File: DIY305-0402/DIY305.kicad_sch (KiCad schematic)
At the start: 37 parts, among them J4 Conn_02x07_Counter_Clockwise

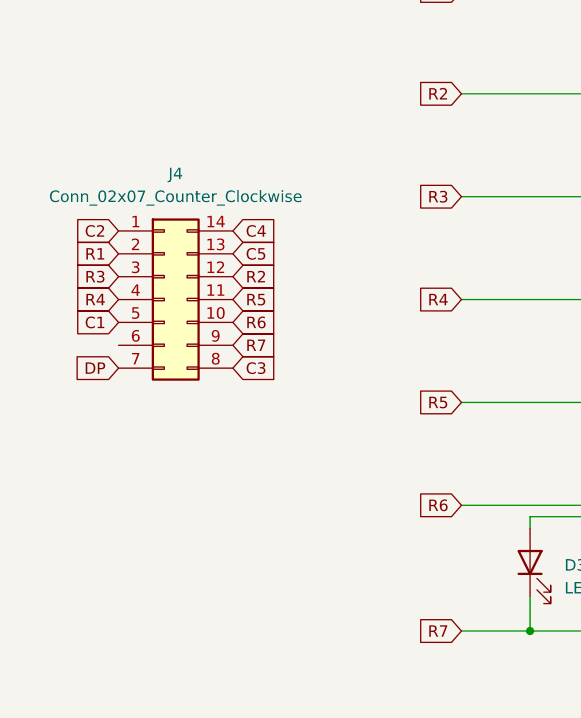
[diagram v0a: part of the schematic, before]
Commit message: Removal of old design
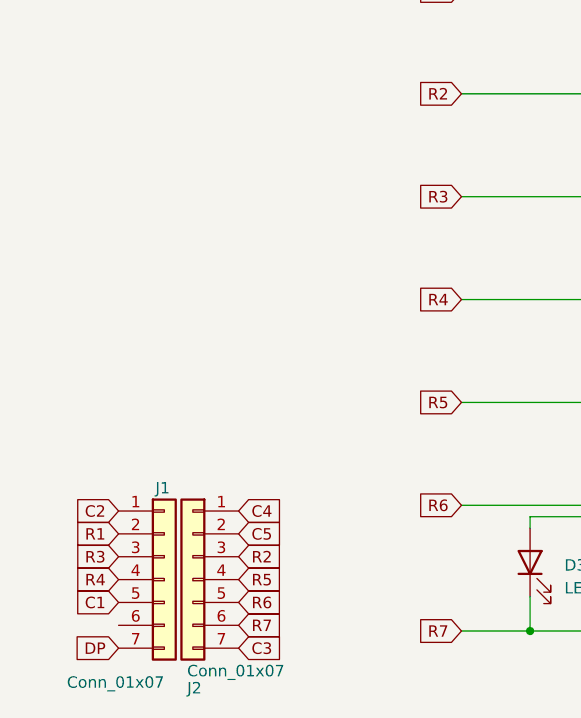
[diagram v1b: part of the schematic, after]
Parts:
- removed J4: Conn_02x07_Counter_Clockwise, symbol Connector_Generic:Conn_02x07_Counter_Clockwise
- added J1, J2: Conn_01x07, Connector_PinHeader_2.54mm:PinHeader_1x07_P2.54mm_Vertical, symbol Connector_Generic:Conn_01x07
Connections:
- net C1: now also J2.5 (Pin_5)
- net C2: now also J2.1 (Pin_1)
- net C3: now also J1.7 (Pin_7)
- net C4: now also J1.1 (Pin_1)
- net C5: now also J1.2 (Pin_2)
- net DP: now also J2.7 (Pin_7)
- net R1: now also J2.2 (Pin_2)
- net R2: now also J1.3 (Pin_3)
- net R3: now also J2.3 (Pin_3)
- net R4: now also J2.4 (Pin_4)
- net R5: now also J1.4 (Pin_4)
- net R6: now also J1.5 (Pin_5)
- net R7: now also J1.6 (Pin_6)

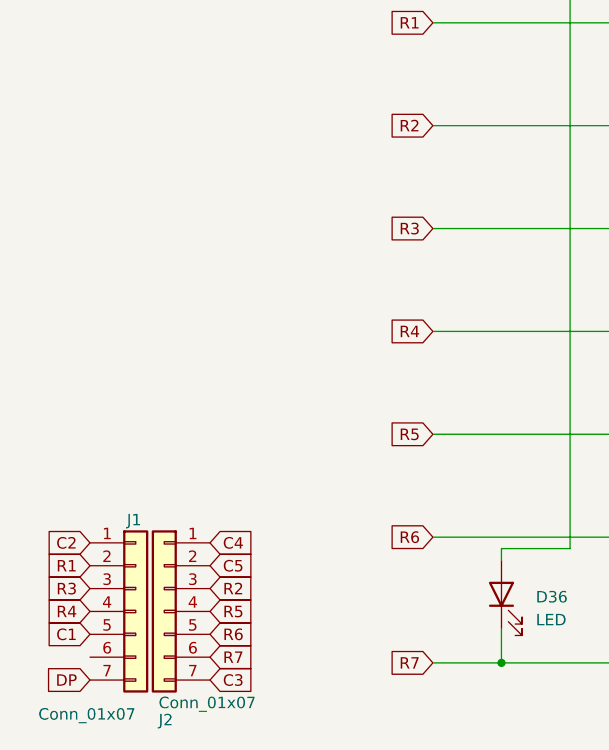
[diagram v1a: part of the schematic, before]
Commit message: Fixed spacing of pins and corrected orientation, made holes bigger and made tracks curvey with teardrops.
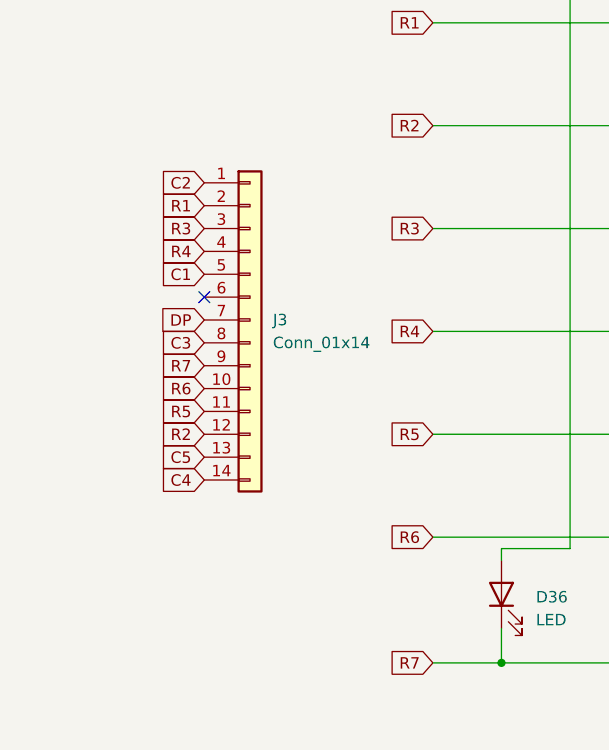
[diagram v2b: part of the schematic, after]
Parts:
- removed J1, J2: Conn_01x07, Connector_PinHeader_2.54mm:PinHeader_1x07_P2.54mm_Vertical, symbol Connector_Generic:Conn_01x07
- added J3: Conn_01x14, Connector_PinHeader_1.00mm:PinHeader_1x14_P1.00mm_Vertical, symbol Connector_Generic:Conn_01x14
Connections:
- net C1: now also J3.5 (Pin_5)
- net C2: now also J3.1 (Pin_1)
- net C3: now also J3.8 (Pin_8)
- net C4: now also J3.14 (Pin_14)
- net C5: now also J3.13 (Pin_13)
- net DP: now also J3.7 (Pin_7)
- net R1: now also J3.2 (Pin_2)
- net R2: now also J3.12 (Pin_12)
- net R3: now also J3.3 (Pin_3)
- net R4: now also J3.4 (Pin_4)
- net R5: now also J3.11 (Pin_11)
- net R6: now also J3.10 (Pin_10)
- net R7: now also J3.9 (Pin_9)
- no-connect marks 0 -> 1
